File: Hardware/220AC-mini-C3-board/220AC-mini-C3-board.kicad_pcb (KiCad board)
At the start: 2 copper layers, 52.7 x 52.7 mm, 16 parts, among them J1 AC MAINS POWER, J2 ON/OFF switch, J4 Conn_01x06_Pin, K1 HF163-F, Q1 Q_NPN_CBE, Q2 Q_NPN_CBE

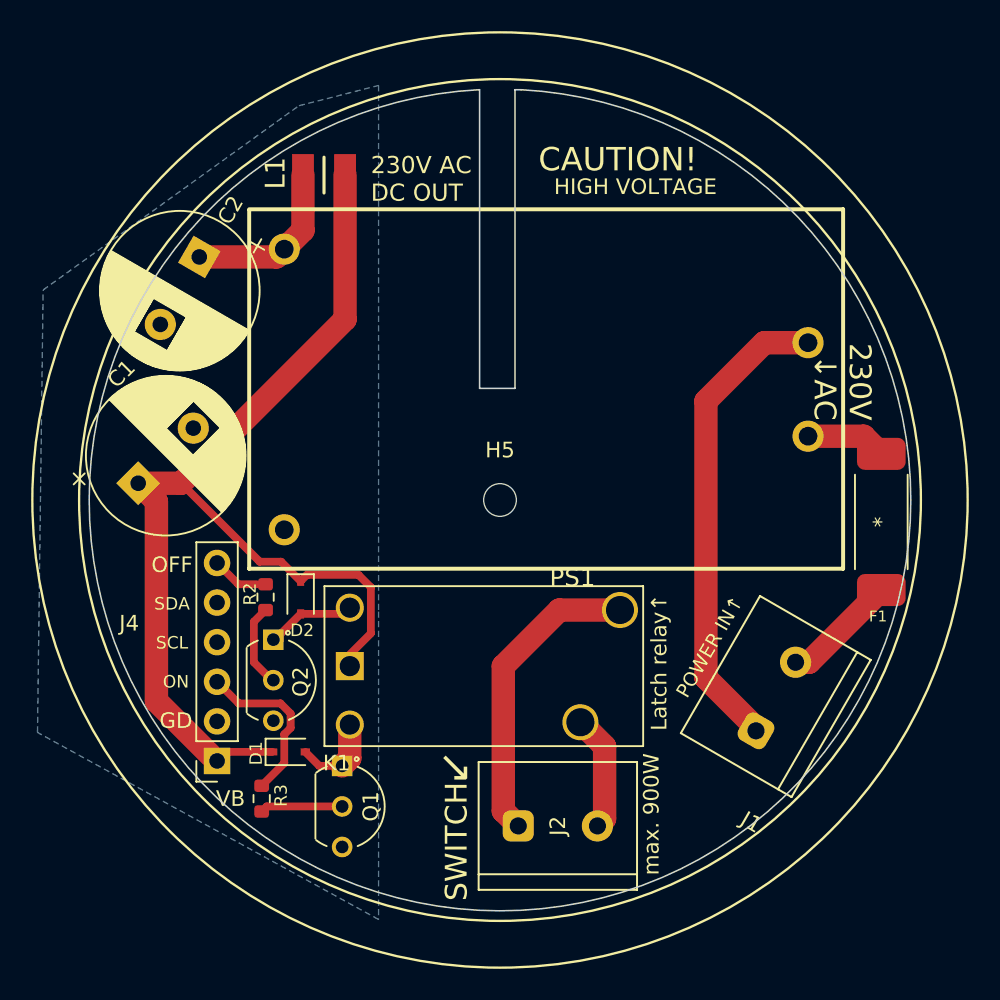
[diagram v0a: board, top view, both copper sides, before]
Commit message: Added Power Sensor connector
Addded Power Sensor ASML115
finished for production
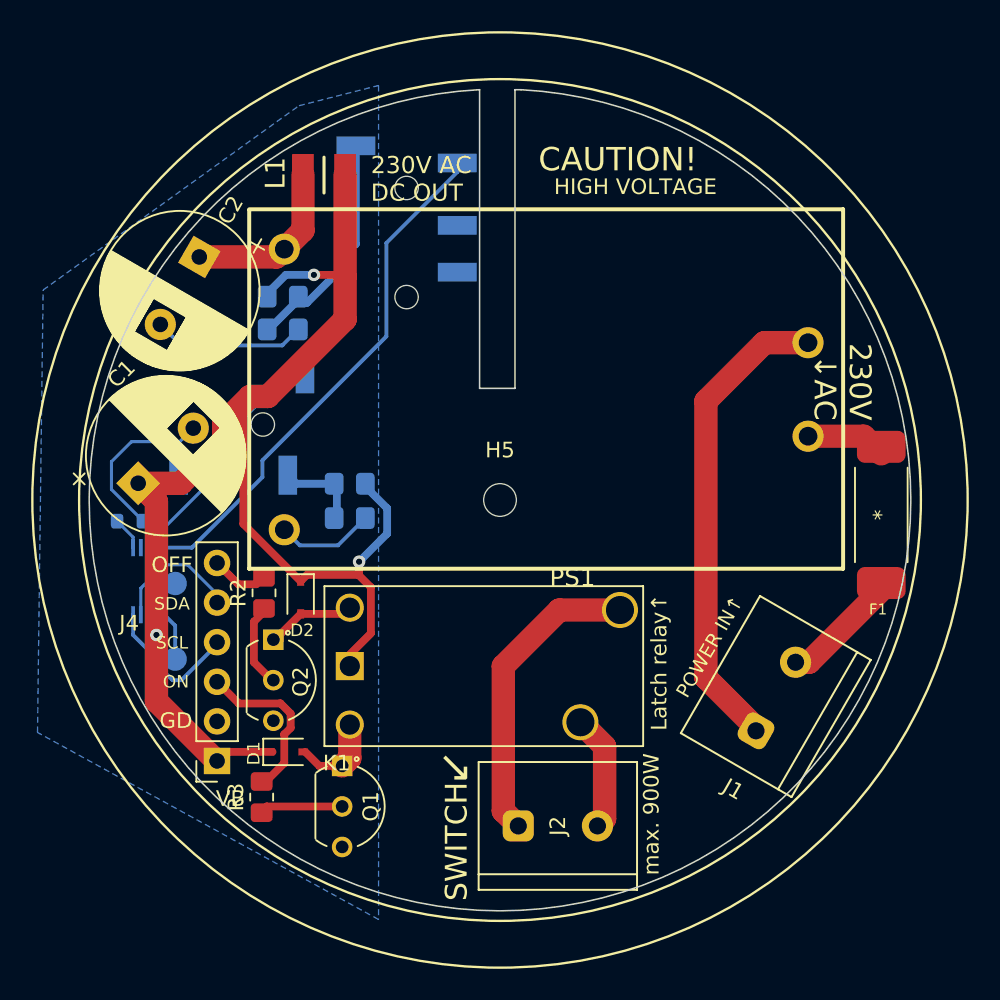
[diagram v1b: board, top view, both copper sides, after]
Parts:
- added J3: AudioJack4, Connector_Audio:Jack_3.5mm_PJ320D_Horizontal, B.Cu at (119.1, 80.5)
- added J6: AudioJack4, Connector_Audio:Jack_3.5mm_PJ320D_Horizontal, B.Cu at (130.5, 67.5)
- added R4: 430Ω, Resistor_SMD:R_0805_2012Metric_Pad1.20x1.40mm_HandSolder, B.Cu at (122.6, 74.4)
- added R5: 430Ω, Resistor_SMD:R_0805_2012Metric_Pad1.20x1.40mm_HandSolder, B.Cu at (122.6, 72.3)
- added R6: 430Ω, Resistor_SMD:R_0805_2012Metric_Pad1.20x1.40mm_HandSolder, B.Cu at (126.9, 86.5)
- added R7: 430Ω, Resistor_SMD:R_0805_2012Metric_Pad1.20x1.40mm_HandSolder, B.Cu at (126.9, 84.3)
- added R8: 19k, Resistor_SMD:R_0603_1608Metric, B.Cu at (112.8, 86.7)
- added TP1: TestPoint, TestPoint:TestPoint_Pad_D1.5mm, B.Cu at (115.7, 95.5)
- added TP2: TestPoint, TestPoint:TestPoint_Pad_D1.5mm, B.Cu at (115.7, 90.7)
- added U2: ADS1115IDGS, Package_SO:TSSOP-10_3x3mm_P0.5mm, B.Cu at (114.0, 90.5)
- R2, R3: footprint Resistor_SMD:R_0603_1608Metric -> Resistor_SMD:R_0805_2012Metric_Pad1.20x1.40mm_HandSolder
- moved F1 0.45 mm to (161.0, 86.3)
- moved R2 0.29 mm to (121.4, 91.3)
- moved D1 0.15 mm to (122.8, 101.5)
- moved R3 0.10 mm to (121.2, 104.4)
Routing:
- net Net-(U2-AIN1): track 0.00 -> 33.5 mm
- net GND: track 0.00 -> 28.8 mm
- net +3V3: track 70.8 -> 89.6 mm, vias 0 -> 3
- net Net-(U2-AIN0): track 0.00 -> 15.9 mm
- net Net-(J6-PadS): track 0.00 -> 14.5 mm
- net /SCL: track 0.00 -> 9.20 mm
- net /SDA: track 0.00 -> 8.53 mm
- net Net-(J3-PadT): track 0.00 -> 5.58 mm
- net Net-(U2-AIN2): track 0.00 -> 2.79 mm
- net Net-(U2-AIN3): track 0.00 -> 2.50 mm
- net Net-(U2-ADDR): track 0.00 -> 2.12 mm
